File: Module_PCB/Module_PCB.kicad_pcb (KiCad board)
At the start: 2 copper layers, 247.5 x 25 mm, 109 parts, among them J2 ISP, J4 DS, J5 US, Q1 KIA50N03B, Q2 KIA50N03B, Q3 KIA50N03B, Q4 KIA50N03B, U1 W25Q16JV, U2 AP1117-33, U3 TPS563200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

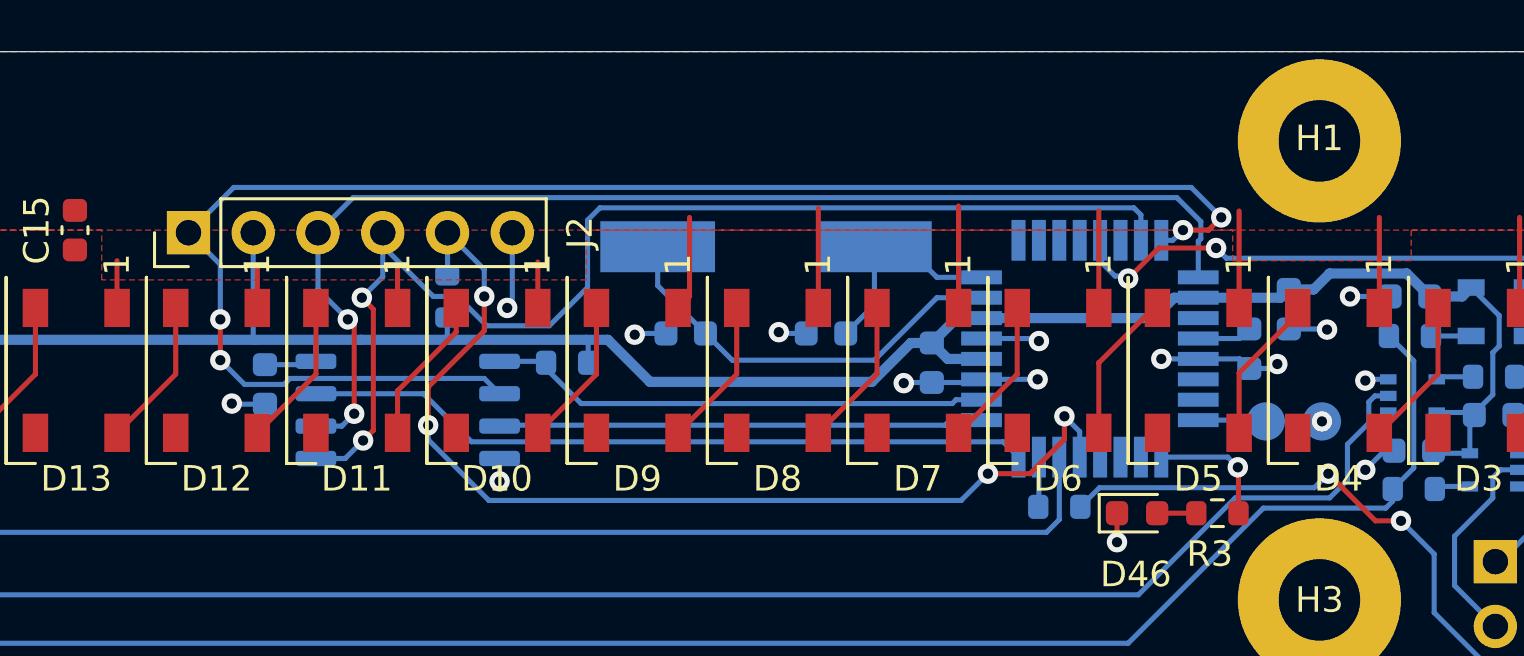
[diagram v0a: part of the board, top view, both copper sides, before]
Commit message: Changed ISP header back to 2x3
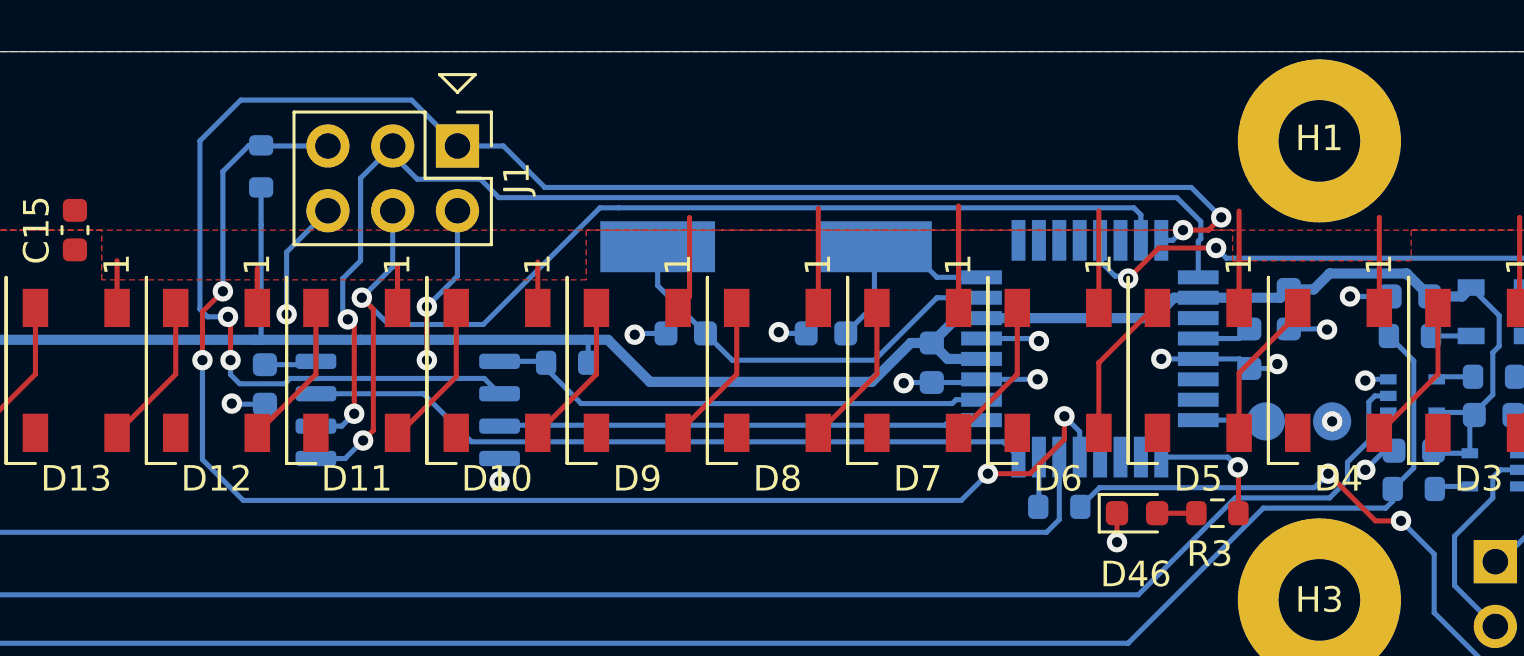
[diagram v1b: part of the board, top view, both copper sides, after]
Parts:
- removed J2: ISP, Connector_PinHeader_2.54mm:PinHeader_1x06_P2.54mm_Vertical
- added J1: ISP, Connector_PinHeader_2.54mm:PinHeader_2x03_P2.54mm_Vertical, F.Cu at (213.7, 103.7)
- moved R1 8.91 mm to (206.0, 104.5)
- moved TP2 0.40 mm to (248.0, 114.5)
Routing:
- net /~RESET: track 41.0 -> 54.4 mm
- net +3V3: track 119.0 -> 127.0 mm, vias 0 -> 2
- net /MISO: track 61.7 -> 66.5 mm
- net GND: track 36.3 -> 38.0 mm
- net /SCK: track 47.2 -> 48.5 mm
- net /MOSI: track 47.1 -> 46.0 mm

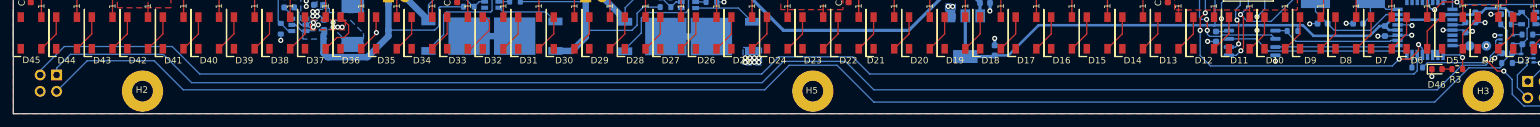
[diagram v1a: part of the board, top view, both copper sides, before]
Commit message: Fixed connector position
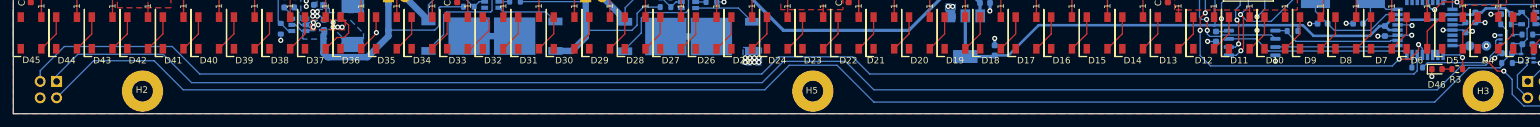
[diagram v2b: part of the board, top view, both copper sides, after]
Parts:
- moved J5 1.00 mm to (26.7, 120.0)
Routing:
- net /RX: track 222.0 -> 223.0 mm

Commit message: Changed the battery protection method and added a turn-on wire for the master
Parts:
- removed BT2: 18650, Connector_PinHeader_2.54mm:PinHeader_1x02_P2.54mm_Vertical
- removed C11, C4: 100n, Capacitor_SMD:C_0603_1608Metric
- removed J4: DS, Connector_PinSocket_2.54mm:PinSocket_2x02_P2.54mm_Horizontal
- removed J5: US, Connector_PinHeader_2.54mm:PinHeader_2x02_P2.54mm_Horizontal
- removed Q3, Q4: KIA50N03B, Package_TO_SOT_SMD:TO-252-2
- removed R10: 2.7k, Resistor_SMD:R_0603_1608Metric
- removed R8: 330, Resistor_SMD:R_0603_1608Metric
- removed U4, U6: AP9101CK6, Package_TO_SOT_SMD:SOT-23-6
- added D47: D_Schottky, Diode_SMD:D_SOD-123, B.Cu at (110.4, 114.3)
- added J2: US, Connector_PinHeader_2.54mm:PinHeader_2x03_P2.54mm_Horizontal, B.Cu at (27.0, 118.0)
- added J3: DS, Connector_PinSocket_2.54mm:PinSocket_2x03_P2.54mm_Horizontal, B.Cu at (254.3, 118.0)
- BT1: value 18650 -> 2x18650; footprint Connector_PinHeader_2.54mm:PinHeader_1x02_P2.54mm_Vertical -> Connector_PinHeader_2.54mm:PinHeader_2x01_P2.54mm_Vertical
- Q1: value KIA50N03B -> HSS2307; footprint Package_TO_SOT_SMD:TO-252-2 -> Package_TO_SOT_SMD:SOT-23
- Q2: value KIA50N03B -> BSS123; footprint Package_TO_SOT_SMD:TO-252-2 -> Package_TO_SOT_SMD:SOT-23
- R2: value 330 -> 10k
- R5: value 2.7k -> 10k
- moved BT1 35.8 mm to (113.9, 107.0), turned to 0 degrees
- moved Q1 20.6 mm to (108.2, 107.0)
- moved R2 17.7 mm to (108.1, 110.5)
- moved R5 13.1 mm to (107.3, 116.5), turned to 180 degrees
- moved Q2 7.62 mm to (107.3, 113.6), turned to 90 degrees
- moved C20 5.07 mm to (254.4, 105.8), turned to 0 degrees
- moved D46 4.05 mm to (242.2, 121.7), turned to 90 degrees
- moved TP2 1.92 mm to (247.7, 112.6)
- moved C18 1.70 mm to (254.3, 112.5)
- moved C19 1.70 mm to (251.2, 114.0)
- moved R11 1.70 mm to (251.2, 115.5)
- moved R12 1.70 mm to (251.1, 109.5)
- moved R13 1.70 mm to (254.3, 111.0)
- moved U7 1.70 mm to (251.2, 111.8)
- moved U8 1.70 mm to (254.3, 114.7)
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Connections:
- BT1 pad 1: +BATT -> /BAT_RAW
- BT1 pad 2: Net-(BT1-Pad2) -> GND
- Q1 pad 1: Net-(Q1-Pad1) -> Net-(D47-Pad2)
- Q1 pad 2: Net-(Q1-Pad2) -> +BATT
- Q1 pad 3: Net-(BT1-Pad2) -> /BAT_RAW
- Q2 pad 1: Net-(Q2-Pad1) -> /PWR_EN
- Q2 pad 2: Net-(Q1-Pad2) -> GND
- Q2 pad 3: Net-(BT2-Pad1) -> Net-(D47-Pad2)
- R2 pad 1: Net-(C4-Pad1) -> /BAT_RAW
- R2 pad 2: +BATT -> Net-(D47-Pad2)
- R5 pad 1: Net-(R5-Pad1) -> /PWR_EN
- R5 pad 2: Net-(BT2-Pad1) -> GND
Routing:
- net /MASTER_ON: track 0.00 -> 246.1 mm, vias 0 -> 2
- net Net-(BT2-Pad1): track 36.9 -> 0.00 mm
- net +BATT: track 138.8 -> 114.0 mm
- net Net-(BT1-Pad2): track 18.2 -> 0.00 mm
- net Net-(BT2-Pad2): track 17.7 -> 0.00 mm
- net Net-(Q1-Pad1): track 17.5 -> 0.00 mm
- net Net-(Q3-Pad1): track 16.9 -> 0.00 mm
- net Net-(Q2-Pad1): track 9.63 -> 0.00 mm
- net Net-(Q4-Pad1): track 9.63 -> 0.00 mm
- net Net-(D47-Pad2): track 0.00 -> 7.81 mm
- net /RX: track 223.0 -> 230.1 mm
- net Net-(Q3-Pad2): track 7.05 -> 0.00 mm
- net Net-(Q1-Pad2): track 7.05 -> 0.00 mm
- net /TX: track 42.3 -> 35.5 mm
- net /RETI: track 8.25 -> 3.82 mm
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- added copper zone on B.Cu, net /BAT_RAW

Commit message: Added a polyfuse, fixes #4
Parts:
- added F1: Polyfuse, Fuse:Fuse_1812_4532Metric_Castellated, B.Cu at (119.6, 107.0)
- moved BT1 10.9 mm to (124.8, 107.0)
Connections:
- BT1 pad 1: /BAT_RAW -> Net-(BT1-Pad1)
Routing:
- net Net-(BT1-Pad1): track 0.00 -> 3.04 mm

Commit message: Added voltage divider to measure the battery voltage
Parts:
- added C4: 100n, Capacitor_SMD:C_0603_1608Metric, B.Cu at (175.5, 111.4)
- added R10: 15k, Resistor_SMD:R_0603_1608Metric, B.Cu at (174.0, 111.4)
- added R8: 10k, Resistor_SMD:R_0603_1608Metric, B.Cu at (174.0, 108.4)
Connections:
- U5 pad 22: Net-(U5-Pad22) -> /REF_BAT
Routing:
- net /REF_BAT: track 0.00 -> 82.3 mm, vias 0 -> 2
- net +BATT: track 114.0 -> 119.4 mm
- net GND: track 41.7 -> 44.2 mm, vias 31 -> 33

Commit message: Routed two signals which were forgotten
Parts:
- moved TP1 0.50 mm to (245.4, 115.0)
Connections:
- U5 pad 12: Net-(U5-Pad12) -> /~RET_EN
- U5 pad 23: Net-(U5-Pad23) -> /TRIGI
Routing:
- net /~RET_EN: track 0.00 -> 31.8 mm, vias 0 -> 4
- net /TRIGI: track 237.2 -> 244.0 mm
- net /REF_BAT: track 82.3 -> 84.6 mm
- net /SCK: track 48.5 -> 49.4 mm
- net /MOSI: track 46.5 -> 47.1 mm

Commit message: Moved the holes of the module PCB for a better mechanically fit
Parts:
- moved H1 35.0 mm to (212.5, 103.5)
- moved H3 35.0 mm to (212.5, 121.5)
- moved C21 11.0 mm to (195.2, 113.0)
- moved J1 11.0 mm to (202.7, 103.7)
- moved R1 11.0 mm to (195.0, 104.5)
- moved R4 11.0 mm to (207.0, 112.2)
- moved U1 11.0 mm to (200.8, 114.0)
- moved C15 4.80 mm to (193.9, 107.0)
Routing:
- net /MISO: track 66.5 -> 81.0 mm
- net /SCK: track 49.4 -> 63.4 mm
- net /~RESET: track 54.4 -> 67.5 mm
- net /~WP: track 18.7 -> 30.9 mm
- net /~HOLD: track 28.6 -> 40.7 mm
- net /MOSI: track 47.1 -> 58.1 mm
- net /~CS: track 19.8 -> 30.8 mm
- net +3V3: track 128.8 -> 139.8 mm
- net /MASTER_ON: track 246.1 -> 249.8 mm
- net /REF_BAT: track 84.6 -> 88.1 mm
- net /RETO: track 238.7 -> 242.2 mm
- net /TRIGI: track 244.0 -> 247.2 mm
- net /RX: track 230.1 -> 232.9 mm
- net /~RET_EN: track 31.8 -> 29.3 mm

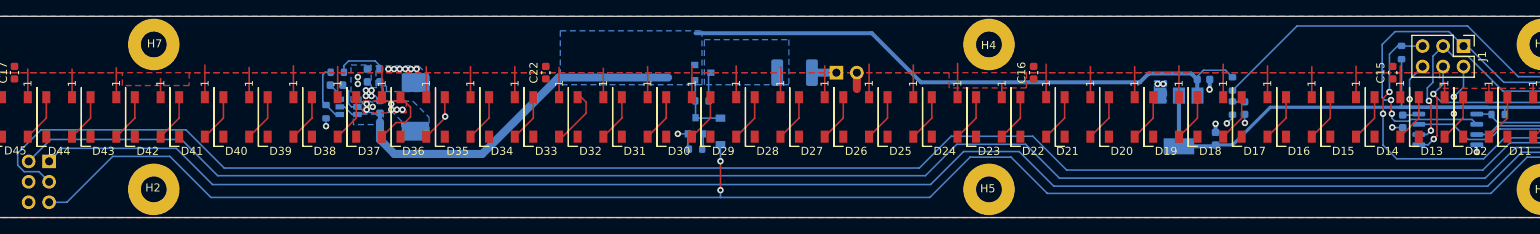
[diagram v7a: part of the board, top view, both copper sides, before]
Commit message: Moved drill holes for better mechanical design
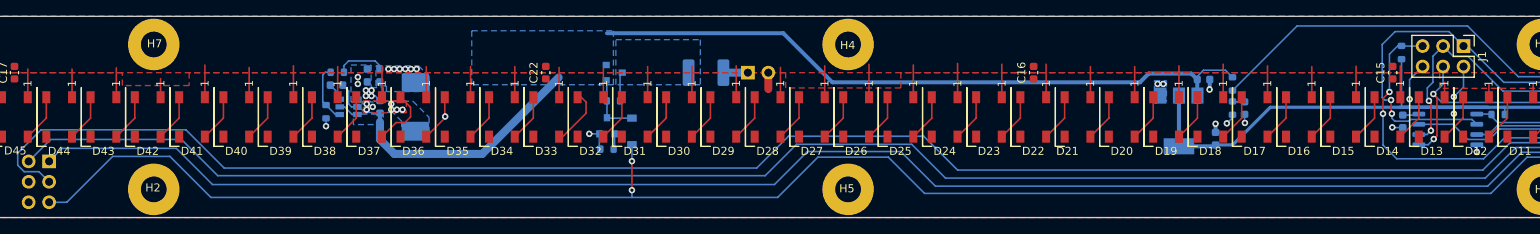
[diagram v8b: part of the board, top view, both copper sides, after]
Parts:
- moved H4 17.5 mm to (126.2, 103.5)
- moved H5 17.5 mm to (126.2, 121.5)
- moved BT1 11.0 mm to (113.8, 107.0)
- moved D47 11.0 mm to (99.4, 114.3)
- moved F1 11.0 mm to (108.6, 107.0)
- moved Q1 11.0 mm to (97.2, 107.0)
- moved Q2 11.0 mm to (96.3, 113.6)
- moved R2 11.0 mm to (97.1, 110.5)
- moved R5 11.0 mm to (96.3, 116.5)
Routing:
- net +BATT: track 119.4 -> 116.8 mm
- net +4V: track 166.7 -> 168.8 mm
